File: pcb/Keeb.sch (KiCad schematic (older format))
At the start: 40 parts, among them J1 TRRS_SJ1-42514, J2 TRRS_SJ1-42514, SW1 SW_RST, U1 ATMEGA32U4, U2 CD74AC138E, U3 CD74AC151E, X1 XTAL_GND

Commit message: Fixed some mistakes in logic/layout from v1
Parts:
- removed J2: TRRS_SJ1-42514, SVastaCustomParts:3.5mm_Cut_out, symbol SVastaCustomParts:TRRS_SJ1-42514
- D500, D501, D502, D503, D504, D505, D506, D507: footprint Keyboard_Parts:D_axial -> Diode_SMD:D_0805_2012Metric_Pad1.15x1.40mm_HandSolder
- R20: footprint Resistor_SMD:R_0805_2012Metric_Pad1.15x1.40mm_HandSolder -> Resistor_THT:R_Axial_DIN0204_L3.6mm_D1.6mm_P5.08mm_Horizontal
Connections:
- net CapsLock: now also U1.27 (T0/PD7); no longer U1.21 (PD3/TXD1)
- net NumLock: now also U1.28 (PB4); no longer U1.22 (PD5/XCK1)
- net SCL: now also J1.2; no longer J1.3
- net SDA: now also J1.3; no longer J1.2
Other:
- moved on the sheet: D401, D402, J1, R19
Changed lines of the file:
@@
 Wire Wire Line
 	6700 4350 6850 4350
-Wire Wire Line
-	9800 1450 9700 1450
-Wire Wire Line
-	9700 1450 9700 1950
-Wire Wire Line
-	9800 1950 9700 1950
-Wire Wire Line
-	9800 1550 9650 1550
-Wire Wire Line
-	9650 1550 9650 2050
-Wire Wire Line
-	9800 2050 9650 2050
-Wire Wire Line
-	9800 1650 9600 1650
-Wire Wire Line
-	9600 1650 9600 2150
-Wire Wire Line
-	9800 2150 9600 2150
-Wire Wire Line
-	9800 1750 9550 1750
-Wire Wire Line
-	9550 1750 9550 2250
-Wire Wire Line
-	9800 2250 9550 2250
-Wire Wire Line
-	9700 1450 9350 1450
-Connection ~ 9700 1450
-Wire Wire Line
-	9650 1550 9350 1550
-Connection ~ 9650 1550
-Wire Wire Line
-	9600 1650 9350 1650
-Connection ~ 9600 1650
-Wire Wire Line
-	9550 1750 9350 1750
-Connection ~ 9550 1750
-Text GLabel 9350 1650 0    50   Input ~ 0
+Text GLabel 9350 1750 0    50   Input ~ 0
 SCL
 Text GLabel 3800 4150 0    50   Input ~ 0
@@
 	3950 4750 3800 4750
 $Comp
-L SVastaCustomParts:TRRS_SJ1-42514 J2
-U 1 1 5D8BAF96
+L SVastaCustomParts:TRRS_SJ1-42514 J1
+U 1 1 5D8C84D5
 P 10050 1300
-F 0 "J2" H 9822 1051 50  0000 R CNN
+F 0 "J1" H 9822 1051 50  0000 R CNN
 F 1 "TRRS_SJ1-42514" H 9822 960 50  0000 R CNN
-F 2 "SVastaCustomParts:3.5mm_Cut_out" H 10050 1300 50  0001 C CNN
+F 2 "SVastaCustomParts:3.5mm_Cut_out" H 10050 700 50  0000 C CNN
 F 3 "https://www.cui.com/product/resource/sj1-4251x-series.pdf" H 10050 1300 50  0001 C CNN
 	1    10050 1300
-	-1   0    0    -1
-$EndComp
-$Comp
-L SVastaCustomParts:TRRS_SJ1-42514 J1
-U 1 1 5D8C84D5
-P 10050 1800
-F 0 "J1" H 9822 1551 50  0000 R CNN
-F 1 "TRRS_SJ1-42514" H 9822 1460 50  0000 R CNN
-F 2 "SVastaCustomParts:3.5mm_Cut_out" H 10050 1800 50  0000 C CNN
-F 3 "https://www.cui.com/product/resource/sj1-4251x-series.pdf" H 10050 1800 50  0001 C CNN
-	1    10050 1800
 	-1   0    0    -1
 $EndComp
@@
 Wire Notes Line
 	9000 1300 11050 1300
-Wire Notes Line
-	11050 1300 11050 3400
-Wire Notes Line
-	11050 3400 9000 3400
-Wire Notes Line
-	9000 3400 9000 1150
 Wire Notes Line
 	9000 1150 10050 1150
@@
 	0    -1   -1   0
 $EndComp
-Text GLabel 9350 1750 0    50   Input ~ 0
+Text GLabel 9350 1650 0    50   Input ~ 0
 SDA
-Text Label 7450 4750 2    50   ~ 0
+Text Label 9950 5100 2    50   ~ 0
 CapsLock
-Text Label 7450 5400 2    50   ~ 0
+Text Label 9950 5750 2    50   ~ 0
 NumLock
 $Comp
@@
 F 0 "R20" V 4650 5450 50  0000 L CNN
 F 1 "10k" V 4550 5500 50  0000 C CNN
-F 2 "Resistor_SMD:R_0805_2012Metric_Pad1.15x1.40mm_HandSolder" V 4480 5500 50  0001 C CNN
+F 2 "Resistor_THT:R_Axial_DIN0204_L3.6mm_D1.6mm_P5.08mm_Horizontal" V 4480 5500 50  0001 C CNN
 F 3 "~" H 4550 5500 50  0001 C CNN
 	1    4550 5500
@@
 F 0 "D504" V 2400 5700 50  0000 L CNN
 F 1 "D" V 2500 5750 50  0000 L CNN
-F 2 "Keyboard_Parts:D_axial" H 2500 5700 50  0001 C CNN
+F 2 "Diode_SMD:D_0805_2012Metric_Pad1.15x1.40mm_HandSolder" H 2500 5700 50  0001 C CNN
 F 3 "~" H 2500 5700 50  0001 C CNN
 	1    2500 5700
@@
 F 0 "D505" V 2650 5700 50  0000 L CNN
 F 1 "D" V 2750 5750 50  0000 L CNN
-F 2 "Keyboard_Parts:D_axial" H 2750 5700 50  0001 C CNN
+F 2 "Diode_SMD:D_0805_2012Metric_Pad1.15x1.40mm_HandSolder" H 2750 5700 50  0001 C CNN
 F 3 "~" H 2750 5700 50  0001 C CNN
 	1    2750 5700
@@
 F 0 "D506" V 2900 5700 50  0000 L CNN
 F 1 "D" V 3000 5750 50  0000 L CNN
-F 2 "Keyboard_Parts:D_axial" H 3000 5700 50  0001 C CNN
+F 2 "Diode_SMD:D_0805_2012Metric_Pad1.15x1.40mm_HandSolder" H 3000 5700 50  0001 C CNN
 F 3 "~" H 3000 5700 50  0001 C CNN
 	1    3000 5700
@@
 F 0 "D507" V 3150 5700 50  0000 L CNN
 F 1 "D" V 3250 5750 50  0000 L CNN
-F 2 "Keyboard_Parts:D_axial" H 3250 5700 50  0001 C CNN
+F 2 "Diode_SMD:D_0805_2012Metric_Pad1.15x1.40mm_HandSolder" H 3250 5700 50  0001 C CNN
 F 3 "~" H 3250 5700 50  0001 C CNN
 	1    3250 5700
@@
 F 0 "D503" V 3400 5700 50  0000 L CNN
 F 1 "D" V 3500 5750 50  0000 L CNN
-F 2 "Keyboard_Parts:D_axial" H 3500 5700 50  0001 C CNN
+F 2 "Diode_SMD:D_0805_2012Metric_Pad1.15x1.40mm_HandSolder" H 3500 5700 50  0001 C CNN
 F 3 "~" H 3500 5700 50  0001 C CNN
 	1    3500 5700
@@
 F 0 "D502" V 3650 5700 50  0000 L CNN
 F 1 "D" V 3750 5750 50  0000 L CNN
-F 2 "Keyboard_Parts:D_axial" H 3750 5700 50  0001 C CNN
+F 2 "Diode_SMD:D_0805_2012Metric_Pad1.15x1.40mm_HandSolder" H 3750 5700 50  0001 C CNN
 F 3 "~" H 3750 5700 50  0001 C CNN
 	1    3750 5700
@@
 F 0 "D501" V 3900 5700 50  0000 L CNN
 F 1 "D" V 4000 5750 50  0000 L CNN
-F 2 "Keyboard_Parts:D_axial" H 4000 5700 50  0001 C CNN
+F 2 "Diode_SMD:D_0805_2012Metric_Pad1.15x1.40mm_HandSolder" H 4000 5700 50  0001 C CNN
 F 3 "~" H 4000 5700 50  0001 C CNN
 	1    4000 5700
@@
 F 0 "D500" V 4150 5700 50  0000 L CNN
 F 1 "D" V 4250 5750 50  0000 L CNN
-F 2 "Keyboard_Parts:D_axial" H 4250 5700 50  0001 C CNN
+F 2 "Diode_SMD:D_0805_2012Metric_Pad1.15x1.40mm_HandSolder" H 4250 5700 50  0001 C CNN
 F 3 "~" H 4250 5700 50  0001 C CNN
 	1    4250 5700
@@
 Wire Wire Line
 	4000 5500 3750 5500
-Connection ~ 8250 5400
-Wire Wire Line
-	8250 4750 8250 5400
-Wire Wire Line
-	8250 5700 8250 5900
+Connection ~ 10750 5750
+Wire Wire Line
+	10750 5100 10750 5750
+Wire Wire Line
+	10750 6050 10750 6250
 $Comp
 L Keyboard_Parts:GND #PWR0145
 U 1 1 5DCEE1A2
-P 8250 5900
-F 0 "#PWR0145" H 8250 5950 20  0001 C CNN
-F 1 "GND" H 8250 5959 30  0000 C CNN
-F 2 "" H 8250 5900 60  0000 C CNN
-F 3 "" H 8250 5900 60  0000 C CNN
-	1    8250 5900
-	1    0    0    -1
-$EndComp
-Wire Wire Line
-	7450 4750 7650 4750
-Wire Wire Line
-	7450 5400 7650 5400
-Wire Wire Line
-	8250 4750 7950 4750
+P 10750 6250
+F 0 "#PWR0145" H 10750 6300 20  0001 C CNN
+F 1 "GND" H 10750 6309 30  0000 C CNN
+F 2 "" H 10750 6250 60  0000 C CNN
+F 3 "" H 10750 6250 60  0000 C CNN
+	1    10750 6250
+	1    0    0    -1
+$EndComp
+Wire Wire Line
+	9950 5100 10150 5100
+Wire Wire Line
+	9950 5750 10150 5750
+Wire Wire Line
+	10750 5100 10450 5100
 $Comp
 L Device:LED D?
 U 1 1 5DC75EFD
-P 7800 4750
+P 10300 5100
 AR Path="/5DF457A9/5DC75EFD" Ref="D?"  Part="1"
 AR Path="/5DC75EFD" Ref="D401"  Part="1"
-F 0 "D401" H 7800 4850 50  0000 C CNN
-F 1 "CAPS" H 7800 4950 50  0000 C CNN
-F 2 "LED_SMD:LED_0805_2012Metric_Pad1.15x1.40mm_HandSolder" H 7800 4750 50  0001 C CNN
-F 3 "~" H 7800 4750 50  0001 C CNN
-	1    7800 4750
+F 0 "D401" H 10300 5200 50  0000 C CNN
+F 1 "CAPS" H 10300 5300 50  0000 C CNN
+F 2 "LED_SMD:LED_0805_2012Metric_Pad1.15x1.40mm_HandSolder" H 10300 5100 50  0001 C CNN
+F 3 "~" H 10300 5100 50  0001 C CNN
+	1    10300 5100
 	-1   0    0    -1
 $EndComp
@@
 L Device:R R?
 U 1 1 5DC64F1A
-P 8250 5550
+P 10750 5900
 AR Path="/5DF457A9/5DC64F1A" Ref="R?"  Part="1"
 AR Path="/5DC64F1A" Ref="R19"  Part="1"
-F 0 "R19" H 8320 5596 50  0000 L CNN
-F 1 "470" V 8250 5450 50  0000 L CNN
-F 2 "Resistor_SMD:R_0805_2012Metric_Pad1.15x1.40mm_HandSolder" V 8180 5550 50  0001 C CNN
-F 3 "~" H 8250 5550 50  0001 C CNN
-	1    8250 5550
-	1    0    0    -1
-$EndComp
-Wire Wire Line
-	8250 5400 7950 5400
+F 0 "R19" H 10820 5946 50  0000 L CNN
+F 1 "470" V 10750 5800 50  0000 L CNN
+F 2 "Resistor_SMD:R_0805_2012Metric_Pad1.15x1.40mm_HandSolder" V 10680 5900 50  0001 C CNN
+F 3 "~" H 10750 5900 50  0001 C CNN
+	1    10750 5900
+	1    0    0    -1
+$EndComp
+Wire Wire Line
+	10750 5750 10450 5750
 $Comp
 L Device:LED D?
 U 1 1 5DC64F13
-P 7800 5400
+P 10300 5750
 AR Path="/5DF457A9/5DC64F13" Ref="D?"  Part="1"
 AR Path="/5DC64F13" Ref="D402"  Part="1"
-F 0 "D402" H 7800 5500 50  0000 C CNN
-F 1 "NUM" H 7800 5600 50  0000 C CNN
-F 2 "LED_SMD:LED_0805_2012Metric_Pad1.15x1.40mm_HandSolder" H 7800 5400 50  0001 C CNN
-F 3 "~" H 7800 5400 50  0001 C CNN
-	1    7800 5400
+F 0 "D402" H 10300 5850 50  0000 C CNN
+F 1 "NUM" H 10300 5950 50  0000 C CNN
+F 2 "LED_SMD:LED_0805_2012Metric_Pad1.15x1.40mm_HandSolder" H 10300 5750 50  0001 C CNN
+F 3 "~" H 10300 5750 50  0001 C CNN
+	1    10300 5750
 	-1   0    0    -1
 $EndComp
@@
 Wire Wire Line
 	4300 4850 4100 4850
-Wire Wire Line
-	4450 4450 4550 4450
-Wire Wire Line
-	4350 4350 4350 4800
-Wire Wire Line
-	4550 4350 4350 4350
-Wire Wire Line
-	4450 4700 4450 4450
-Wire Wire Line
-	4550 4700 4450 4700
-Wire Wire Line
-	4350 4800 4550 4800
-Text Label 4550 4800 0    50   ~ 0
+Text Label 7300 4050 0    50   ~ 0
 CapsLock
-Text Label 4550 4700 0    50   ~ 0
+Text Label 7300 3950 0    50   ~ 0
 NumLock
+Wire Wire Line
+	9350 1450 9800 1450
+Wire Wire Line
+	9350 1550 9800 1550
+Wire Wire Line
+	9350 1650 9800 1650
+Wire Wire Line
+	9350 1750 9800 1750
+Wire Notes Line
+	11050 1300 11050 2000
+Wire Notes Line
+	11050 2000 9000 2000
+Wire Notes Line
+	9000 2000 9000 1150
+Wire Wire Line
+	6700 3950 7300 3950
+Wire Wire Line
+	7300 4050 6700 4050
 $EndSCHEMATC

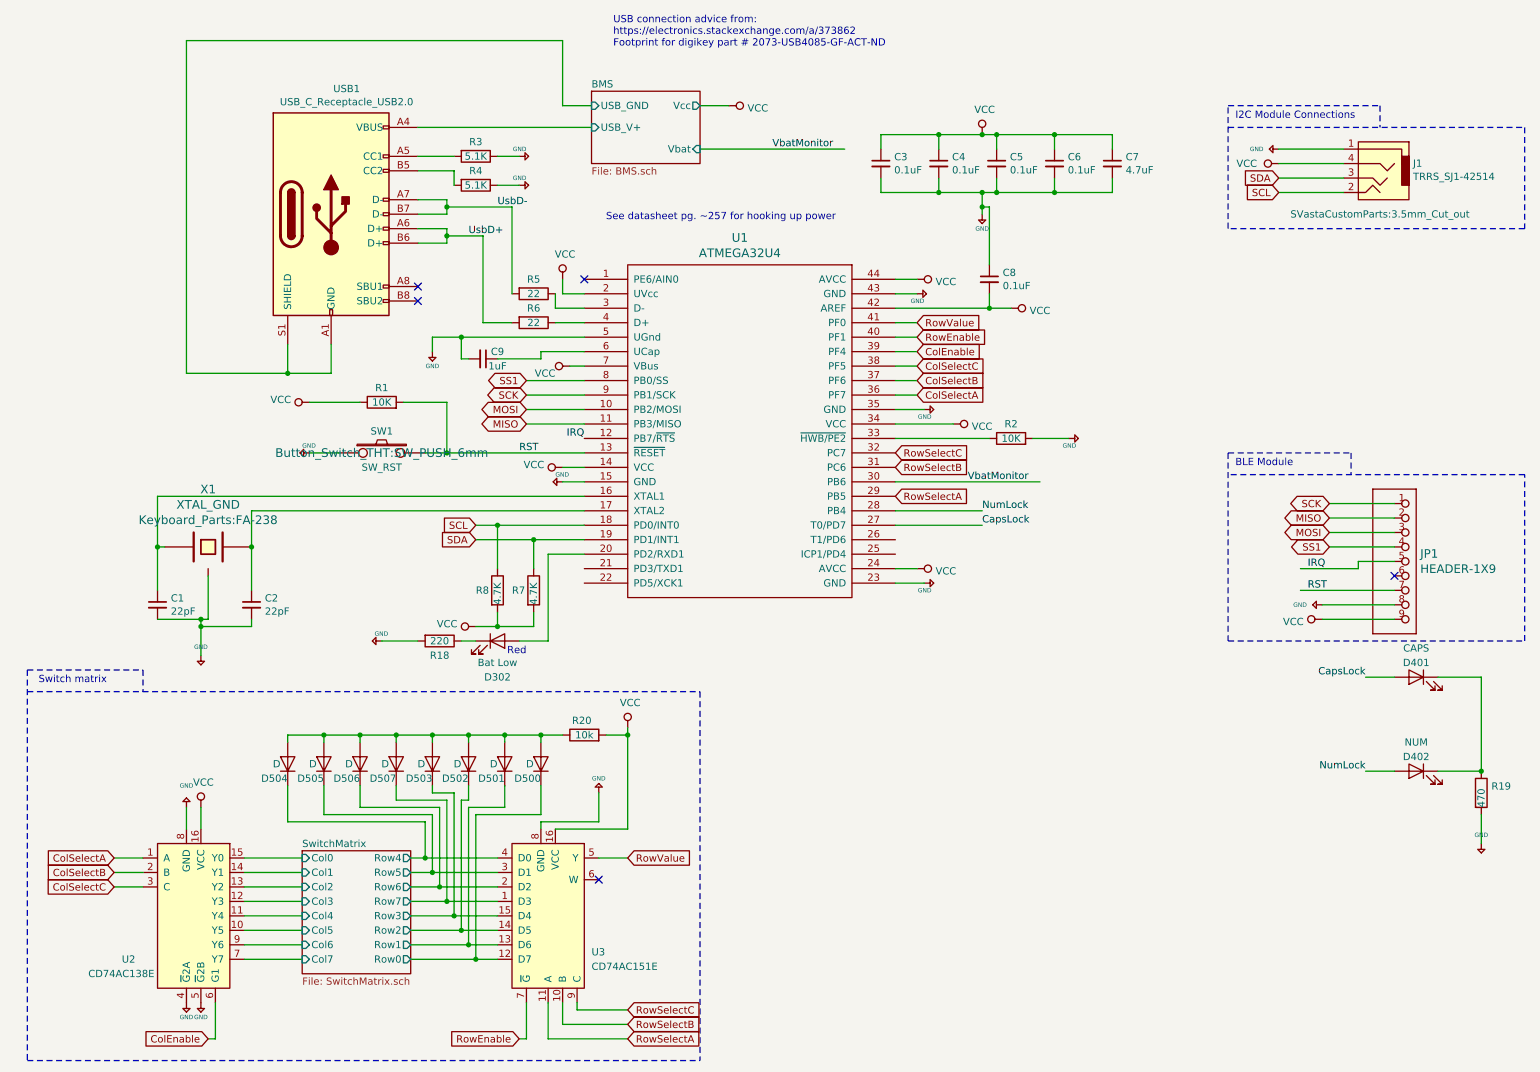
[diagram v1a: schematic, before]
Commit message: Most pcb of layout done
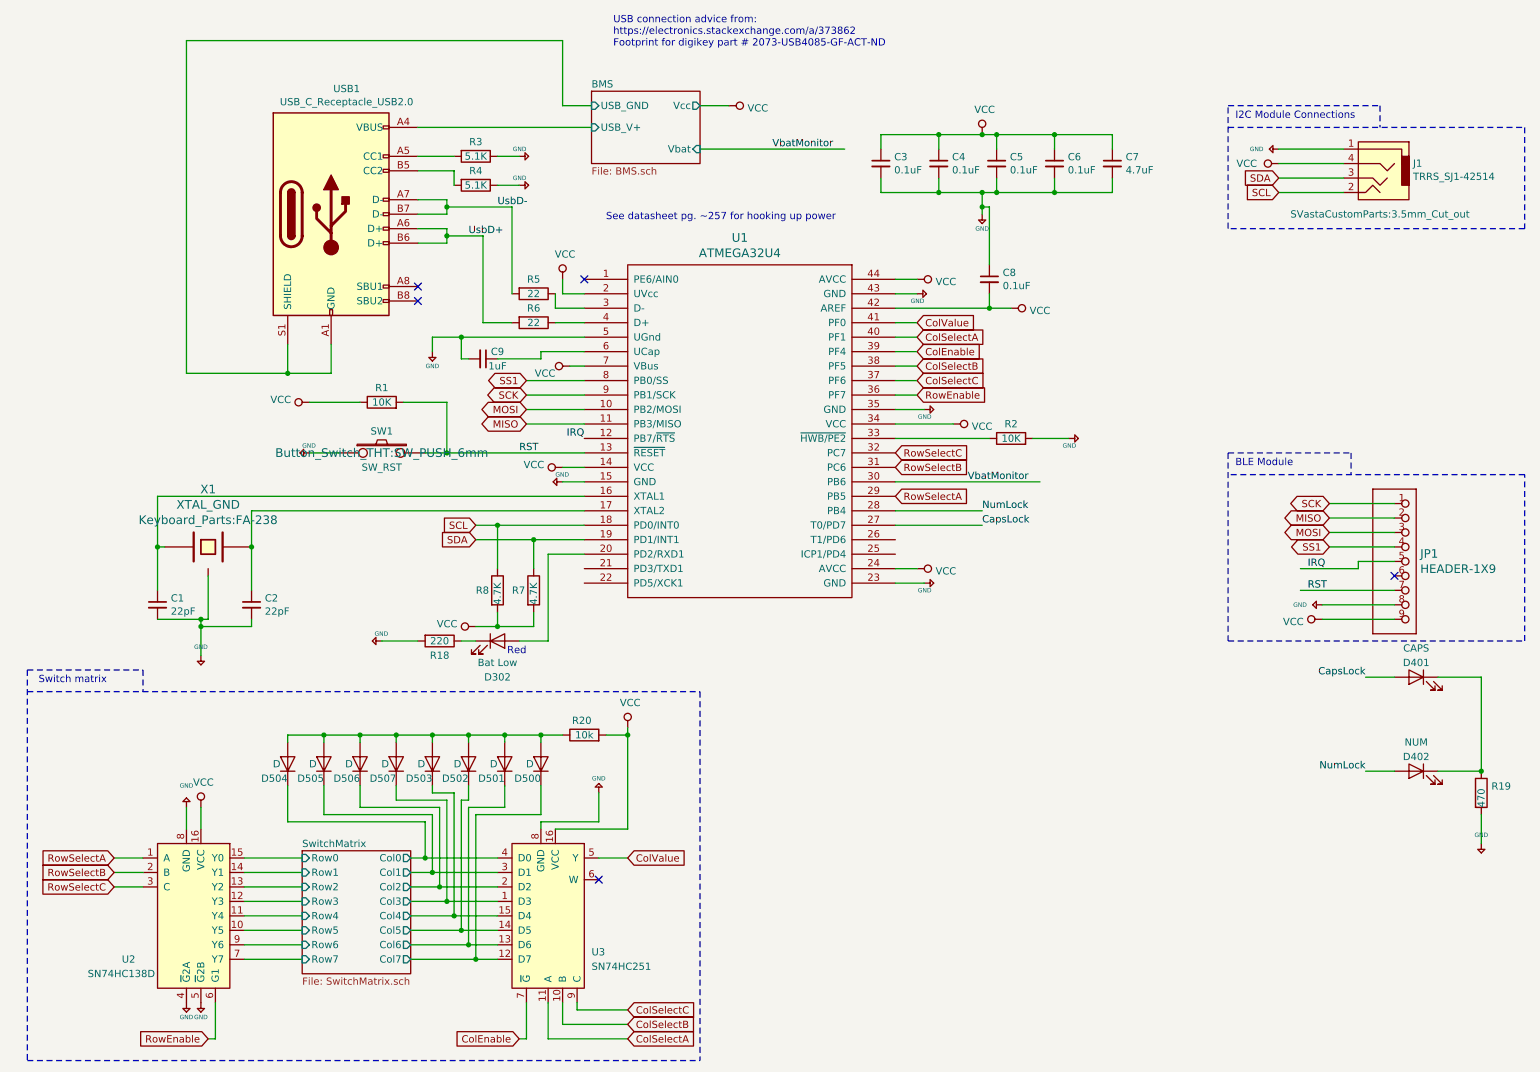
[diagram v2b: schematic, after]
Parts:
- U2: value CD74AC138E -> SN74HC138D‎; footprint SVastaCustomParts:CD74AC151_DIP-16 -> SVastaCustomParts:SN74HC_package_d_soic
- U3: value CD74AC151E -> SN74HC251; footprint SVastaCustomParts:CD74AC151_DIP-16 -> SVastaCustomParts:SN74HC_package_d_soic
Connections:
- net ColEnable: now also U3.7 (~G); no longer U2.6 (G1)
- net ColSelectA: now also U1.40 (PF1), U3.11 (A); no longer U1.36 (PF7), U2.1 (A)
- net ColSelectB: now also U1.38 (PF5), U3.10 (B); no longer U1.37 (PF6), U2.2 (B)
- net ColSelectC: now also U1.37 (PF6), U3.9 (C); no longer U1.38 (PF5), U2.3 (C)
- net RowEnable: now also U1.36 (PF7), U2.6 (G1); no longer U1.40 (PF1), U3.7 (~G)
- net RowSelectA: now also U2.1 (A); no longer U3.11 (A)
- net RowSelectB: now also U2.2 (B); no longer U3.10 (B)
- net RowSelectC: now also U2.3 (C); no longer U3.9 (C)
- net SwitchMatrix/Col0: now also D504.1 (K), U3.4 (D0); no longer U2.15 (Y0)
- net SwitchMatrix/Col1: now also D505.1 (K), U3.3 (D1); no longer U2.14 (Y1)
- net SwitchMatrix/Col2: now also D506.1 (K), U3.2 (D2); no longer U2.13 (Y2)
- net SwitchMatrix/Col3: now also D507.1 (K), U3.1 (D3); no longer U2.12 (Y3)
- net SwitchMatrix/Col4: now also D503.1 (K), U3.15 (D4); no longer U2.11 (Y4)
- net SwitchMatrix/Col5: now also D502.1 (K), U3.14 (D5); no longer U2.10 (Y5)
- net SwitchMatrix/Col6: now also D501.1 (K), U3.13 (D6); no longer U2.9 (Y6)
- net SwitchMatrix/Col7: now also D500.1 (K), U3.12 (D7); no longer U2.7 (Y7)
- net SwitchMatrix/Row0: now also U2.15 (Y0); no longer D500.1 (K), U3.12 (D7)
- net SwitchMatrix/Row1: now also U2.14 (Y1); no longer D501.1 (K), U3.13 (D6)
- net SwitchMatrix/Row2: now also U2.13 (Y2); no longer D502.1 (K), U3.14 (D5)
- net SwitchMatrix/Row3: now also U2.12 (Y3); no longer D503.1 (K), U3.15 (D4)
- net SwitchMatrix/Row4: now also U2.11 (Y4); no longer D504.1 (K), U3.4 (D0)
- net SwitchMatrix/Row5: now also U2.10 (Y5); no longer D505.1 (K), U3.3 (D1)
- net SwitchMatrix/Row6: now also U2.9 (Y6); no longer D506.1 (K), U3.2 (D2)
- net SwitchMatrix/Row7: now also U2.7 (Y7); no longer D507.1 (K), U3.1 (D3)
- net RowValue renamed ColValue
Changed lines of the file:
@@
 P 1850 6200
 F 0 "U2" H 1400 5350 50  0000 C CNN
-F 1 "CD74AC138E" H 1350 5250 50  0000 C CNN
-F 2 "SVastaCustomParts:CD74AC151_DIP-16" H 1850 6200 50  0001 C CNN
-F 3 "http://www.ti.com/lit/ds/symlink/cd74ac138.pdf" H 1850 6200 50  0001 C CNN
+F 1 "SN74HC138D‎" H 1350 5250 50  0000 C CNN
+F 2 "SVastaCustomParts:SN74HC_package_d_soic" H 1850 6200 50  0001 C CNN
+F 3 "http://www.ti.com/lit/ds/symlink/sn74hc138.pdf" H 1850 6200 50  0001 C CNN
 	1    1850 6200
 	1    0    0    -1
@@
 	-1   0    0    1
 $EndComp
-Text GLabel 1300 6350 0    50   Input ~ 0
+Text GLabel 4850 7600 2    50   Input ~ 0
 ColSelectA
-Text GLabel 1300 6450 0    50   Input ~ 0
+Text GLabel 4850 7500 2    50   Input ~ 0
 ColSelectB
-Text GLabel 1300 6550 0    50   Input ~ 0
+Text GLabel 4850 7400 2    50   Input ~ 0
 ColSelectC
 Wire Wire Line
@@
 RST
 Text GLabel 6850 2650 2    50   Input ~ 0
-RowValue
+ColValue
 Text Label 9550 4350 0    50   ~ 0
 IRQ
@@
 Wire Wire Line
 	6850 2950 6700 2950
+Text GLabel 6850 3050 2    50   Input ~ 0
+ColSelectC
 Text GLabel 6850 2950 2    50   Input ~ 0
-ColSelectC
-Text GLabel 6850 3050 2    50   Input ~ 0
 ColSelectB
-Text GLabel 6850 3150 2    50   Input ~ 0
+Text GLabel 6850 2750 2    50   Input ~ 0
 ColSelectA
 Wire Wire Line
@@
 Wire Wire Line
 	1600 4200 1600 4500
-$Sheet
-S 2600 6300 750  850
-U 5D9DA1AD
-F0 "SwitchMatrix" 50
-F1 "SwitchMatrix.sch" 50
-F2 "Row1" O R 3350 6950 50
-F3 "Row2" O R 3350 6850 50
-F4 "Row3" O R 3350 6750 50
-F5 "Row7" O R 3350 6650 50
-F6 "Row6" O R 3350 6550 50
-F7 "Row5" O R 3350 6450 50
-F8 "Row4" O R 3350 6350 50
-F9 "Col0" I L 2600 6350 50
-F10 "Col2" I L 2600 6550 50
-F11 "Col1" I L 2600 6450 50
-F12 "Col3" I L 2600 6650 50
-F13 "Col4" I L 2600 6750 50
-F14 "Col5" I L 2600 6850 50
-F15 "Col6" I L 2600 6950 50
-F16 "Col7" I L 2600 7050 50
-F17 "Row0" O R 3350 7050 50
-$EndSheet
 $Comp
 L Device:C_Small C8
@@
 Wire Notes Line
 	5350 5200 5350 7750
-Text GLabel 1950 7600 0    50   Input ~ 0
+Text GLabel 4100 7600 0    50   Input ~ 0
 ColEnable
 $Comp
@@
 Wire Wire Line
 	2000 7600 2000 7350
-Text GLabel 4100 7600 0    50   Input ~ 0
+Text GLabel 1950 7600 0    50   Input ~ 0
 RowEnable
 Wire Wire Line
@@
 P 4300 6200
 F 0 "U3" H 4600 5400 50  0000 L CNN
-F 1 "CD74AC151E" H 4600 5300 50  0000 L CNN
-F 2 "SVastaCustomParts:CD74AC151_DIP-16" H 4300 6200 50  0001 C CNN
-F 3 "http://www.ti.com/lit/ds/symlink/cd74ac151.pdf" H 4300 6200 50  0001 C CNN
+F 1 "SN74HC251" H 4600 5300 50  0000 L CNN
+F 2 "SVastaCustomParts:SN74HC_package_d_soic" H 4300 6200 50  0001 C CNN
+F 3 "http://www.ti.com/lit/ds/symlink/sn74hc251.pdf" H 4300 6200 50  0001 C CNN
 	1    4300 6200
 	1    0    0    -1
@@
 	0    -1   -1   0
 $EndComp
-Text GLabel 6850 2750 2    50   Input ~ 0
+Text GLabel 6850 3150 2    50   Input ~ 0
 RowEnable
 Text GLabel 6850 2850 2    50   Input ~ 0
@@
 	-1   0    0    -1
 $EndComp
-Text GLabel 4850 7600 2    50   Input ~ 0
+Text GLabel 1300 6350 0    50   Input ~ 0
 RowSelectA
-Text GLabel 4850 7500 2    50   Input ~ 0
+Text GLabel 1300 6450 0    50   Input ~ 0
 RowSelectB
-Text GLabel 4850 7400 2    50   Input ~ 0
+Text GLabel 1300 6550 0    50   Input ~ 0
 RowSelectC
 Text GLabel 4850 6350 2    50   Input ~ 0
-RowValue
+ColValue
 Wire Wire Line
 	3700 4850 3800 4850
@@
 Wire Wire Line
 	7300 4050 6700 4050
+$Sheet
+S 2600 6300 750  850
+U 5D9DA1AD
+F0 "SwitchMatrix" 50
+F1 "SwitchMatrix.sch" 50
+F2 "Row0" I L 2600 6350 50
+F3 "Row7" I L 2600 7050 50
+F4 "Row6" I L 2600 6950 50
+F5 "Row5" I L 2600 6850 50
+F6 "Row4" I L 2600 6750 50
+F7 "Col7" O R 3350 7050 50
+F8 "Row1" I L 2600 6450 50
+F9 "Row2" I L 2600 6550 50
+F10 "Row3" I L 2600 6650 50
+F11 "Col0" O R 3350 6350 50
+F12 "Col1" O R 3350 6450 50
+F13 "Col2" O R 3350 6550 50
+F14 "Col3" O R 3350 6650 50
+F15 "Col4" O R 3350 6750 50
+F16 "Col5" O R 3350 6850 50
+F17 "Col6" O R 3350 6950 50
+$EndSheet
 $EndSCHEMATC

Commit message: Moved custom symbols & footprints into git submodules
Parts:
- JP1: footprint SVastaCustomParts:Adafruit BLE SPI -> SVastaCustomParts:Adafruit_BLE_SPI_wire_tht; symbol Tutorial-eagle-import:HEADER-1X9 -> Connector:Conn_01x09_Female
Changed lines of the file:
@@
 $EndComp
 $Comp
-L Tutorial-eagle-import:HEADER-1X9 JP1
+L Connector:Conn_01x09_Female JP1
 U 1 1 5D8CAFE9
-P 10250 4300
-F 0 "JP1" H 10328 4353 59  0000 L CNN
-F 1 "HEADER-1X9" H 10328 4248 59  0000 L CNN
-F 2 "SVastaCustomParts:Adafruit BLE SPI" H 10250 4300 50  0001 C CNN
-F 3 "" H 10250 4300 50  0001 C CNN
-	1    10250 4300
+P 10350 4300
+F 0 "JP1" H 10428 4353 59  0000 L CNN
+F 1 "HEADER-1X9" H 10428 4248 59  0000 L CNN
+F 2 "SVastaCustomParts:Adafruit_BLE_SPI_wire_tht" H 10350 4300 50  0001 C CNN
+F 3 "" H 10350 4300 50  0001 C CNN
+	1    10350 4300
 	1    0    0    -1
 $EndComp
